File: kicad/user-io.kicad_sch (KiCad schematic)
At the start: 8 parts, among them J1 USB1, SW1 PTS815, U1 MIMXRT1171DVMAB, U2 MAYA-W166-00B

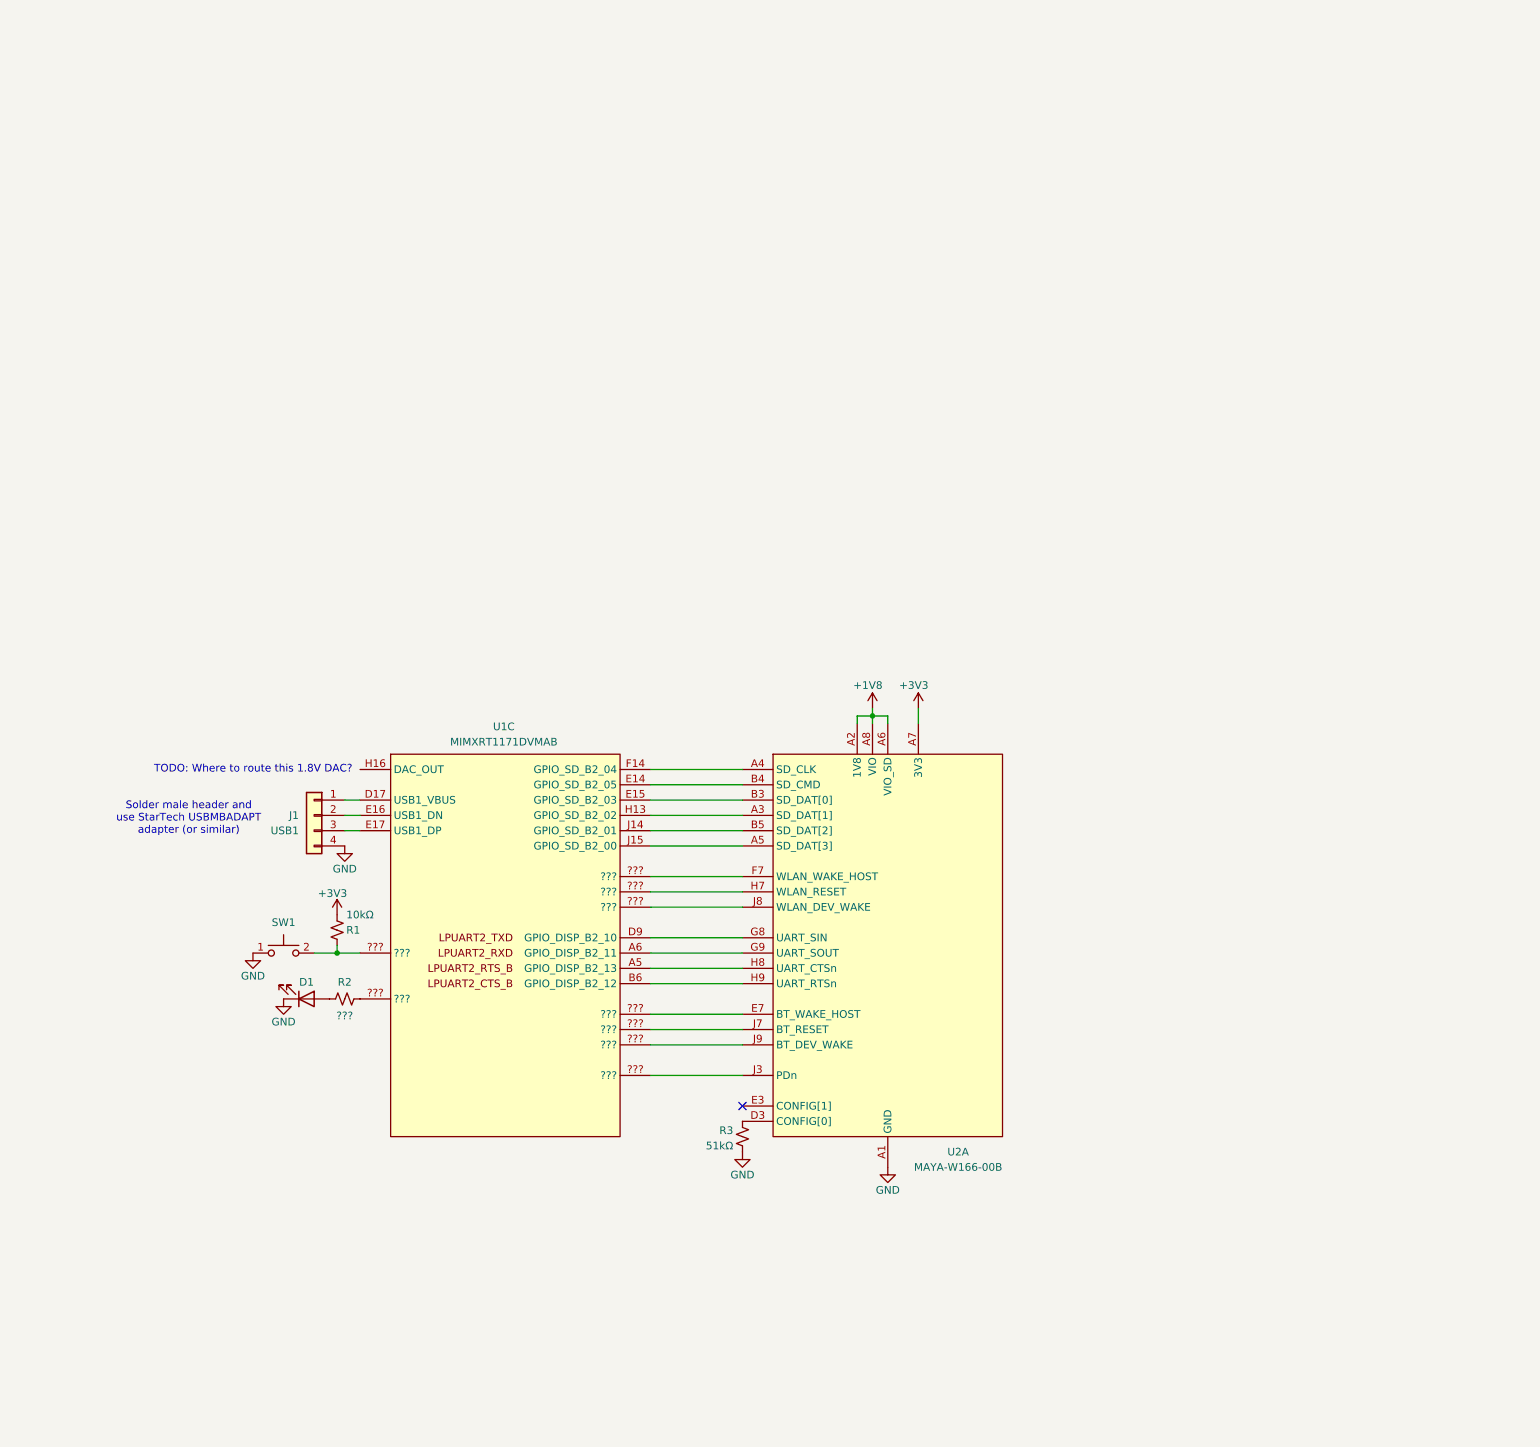
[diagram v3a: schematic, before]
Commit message: added IMU to schematic
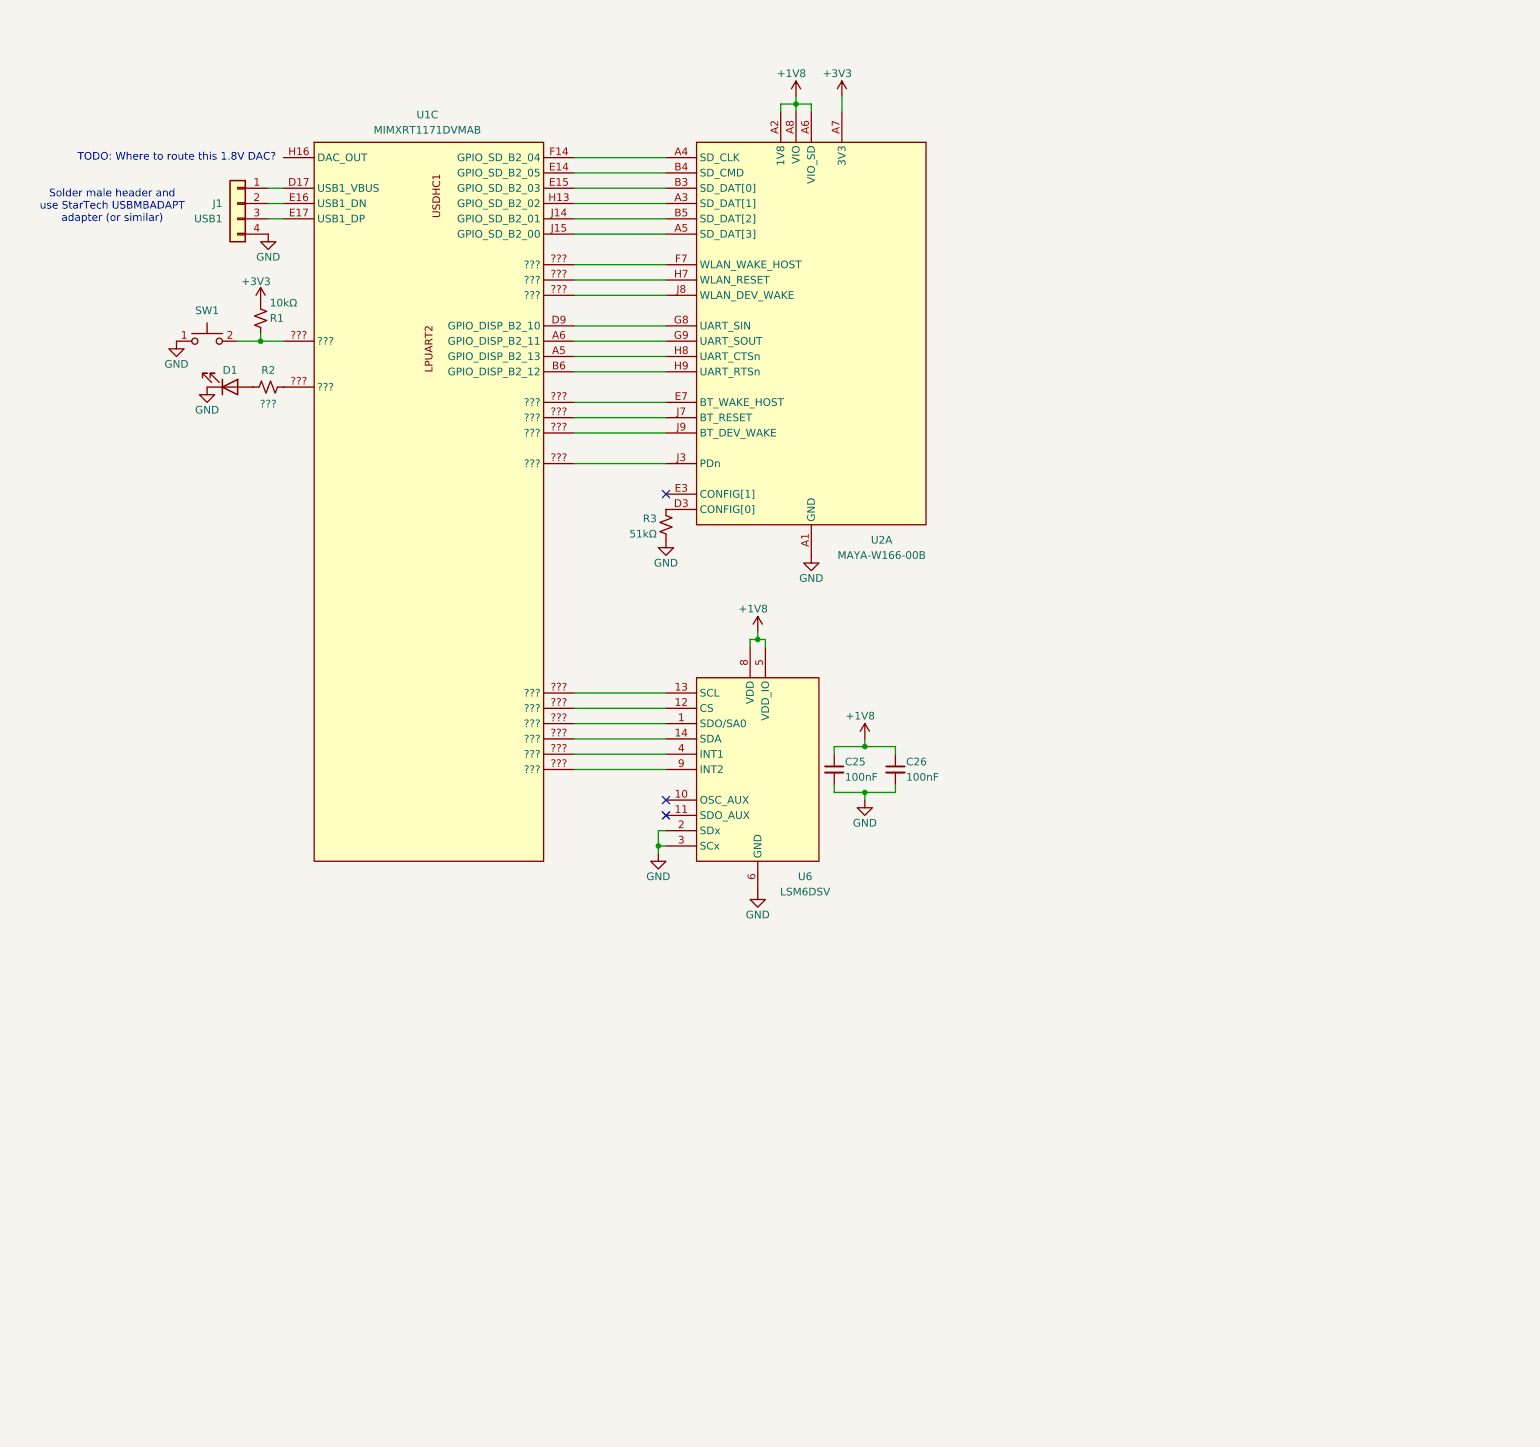
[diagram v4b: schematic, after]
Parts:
- added C25, C26: 100nF, symbol Device:C_Small
- added U6: LSM6DSV, symbol project_symbols:LSM6DSV
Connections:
- net +1V8: now also C25.1, C26.1, U6.5 (VDD_IO), U6.8 (VDD)
- net GND: now also C25.2, C26.2, U6.2 (SDx), U6.3 (SCx), U6.6 (GND), U6.7 (GND)
- new net: U1.???, U6.1 (SDO/SA0)
- new net: U1.???, U6.12 (CS)
- new net: U1.???, U6.13 (SCL)
- new net: U1.???, U6.14 (SDA)
- new net: U1.???, U6.4 (INT1)
- new net: U1.???, U6.9 (INT2)
- no-connect marks 1 -> 3
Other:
- moved on the sheet: D1, J1, R1, R2, R3, SW1, U2A

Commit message: added magnetometer to schematic
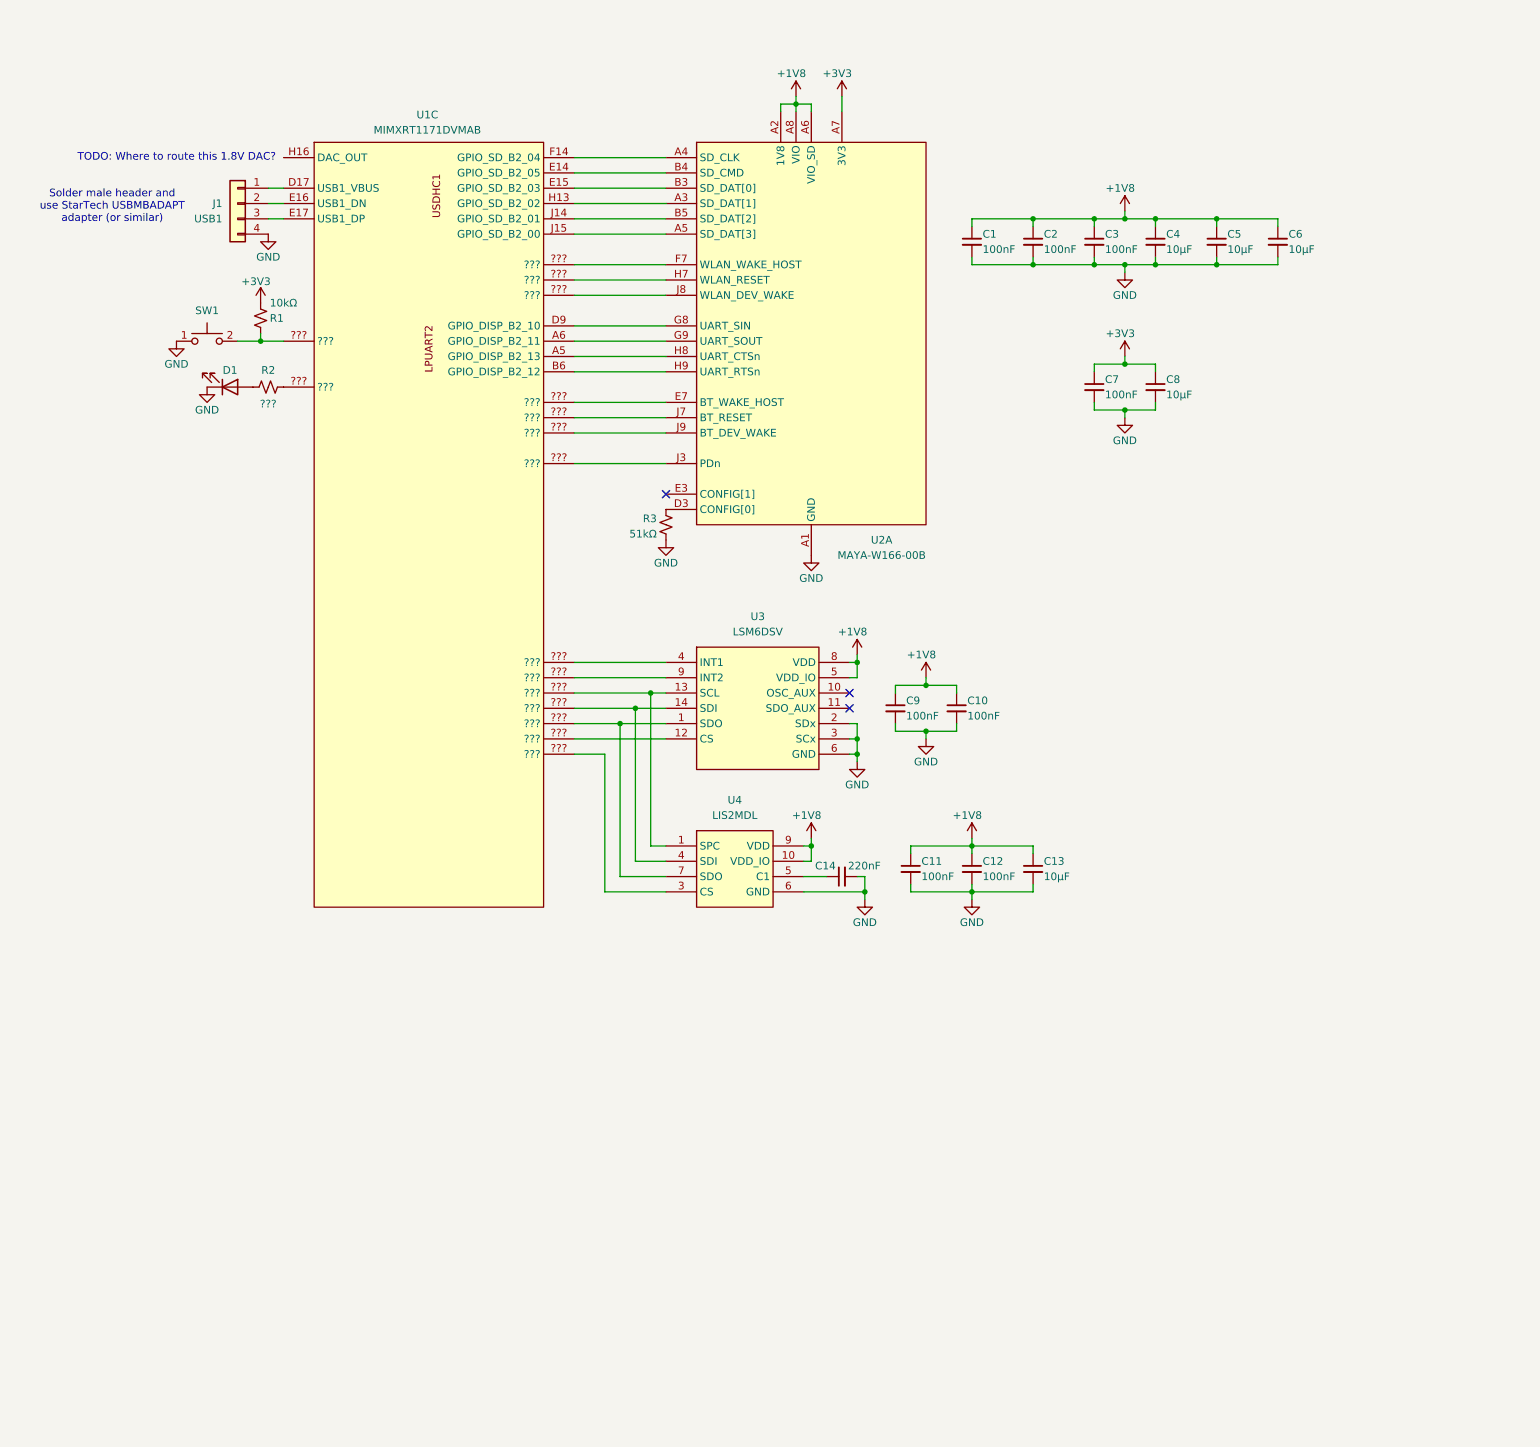
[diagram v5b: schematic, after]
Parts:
- removed U6: LSM6DSV, symbol project_symbols:LSM6DSV
- added C1, C11, C12, C2, C3, C7: 100nF, symbol Device:C_Small
- added C13, C4, C5, C6, C8: 10μF, symbol Device:C_Small
- added C14: 220nF, symbol Device:C_Small
- added U3: LSM6DSV, symbol project_symbols:LSM6DSV
- added U4: LIS2MDL, symbol project_symbols:LIS2MDL
- renumbered C26 to C10, C25 to C9
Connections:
- net +1V8: now also C1.1, C11.1, C12.1, C13.1, C2.1, C3.1, C4.1, C5.1, C6.1, U3.5 (VDD_IO), U3.8 (VDD), U4.10 (VDD_IO), U4.9 (VDD)
- net +3V3: now also C7.1, C8.1
- net GND: now also C1.2, C11.2, C12.2, C13.2, C14.2, C2.2, C3.2, C4.2, C5.2, C6.2, C7.2, C8.2, U3.2 (SDx), U3.3 (SCx), U3.6 (GND), U3.7 (GND), U4.6 (GND), U4.8 (GND)
- net at U1.???: now also U2.J9 (BT_DEV_WAKE)
- new net: U1.???, U3.1 (SDO), U4.7 (SDO)
- new net: U1.???, U3.12 (CS)
- new net: U1.???, U3.13 (SCL), U4.1 (SPC)
- new net: U1.???, U3.14 (SDI), U4.4 (SDI)
- new net: U1.???, U3.4 (INT1)
- new net: U1.???, U3.9 (INT2)
- new net: C14.1, U4.5 (C1)
- new net: U1.???, U4.3 (CS)
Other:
- moved on the sheet: C10, C9

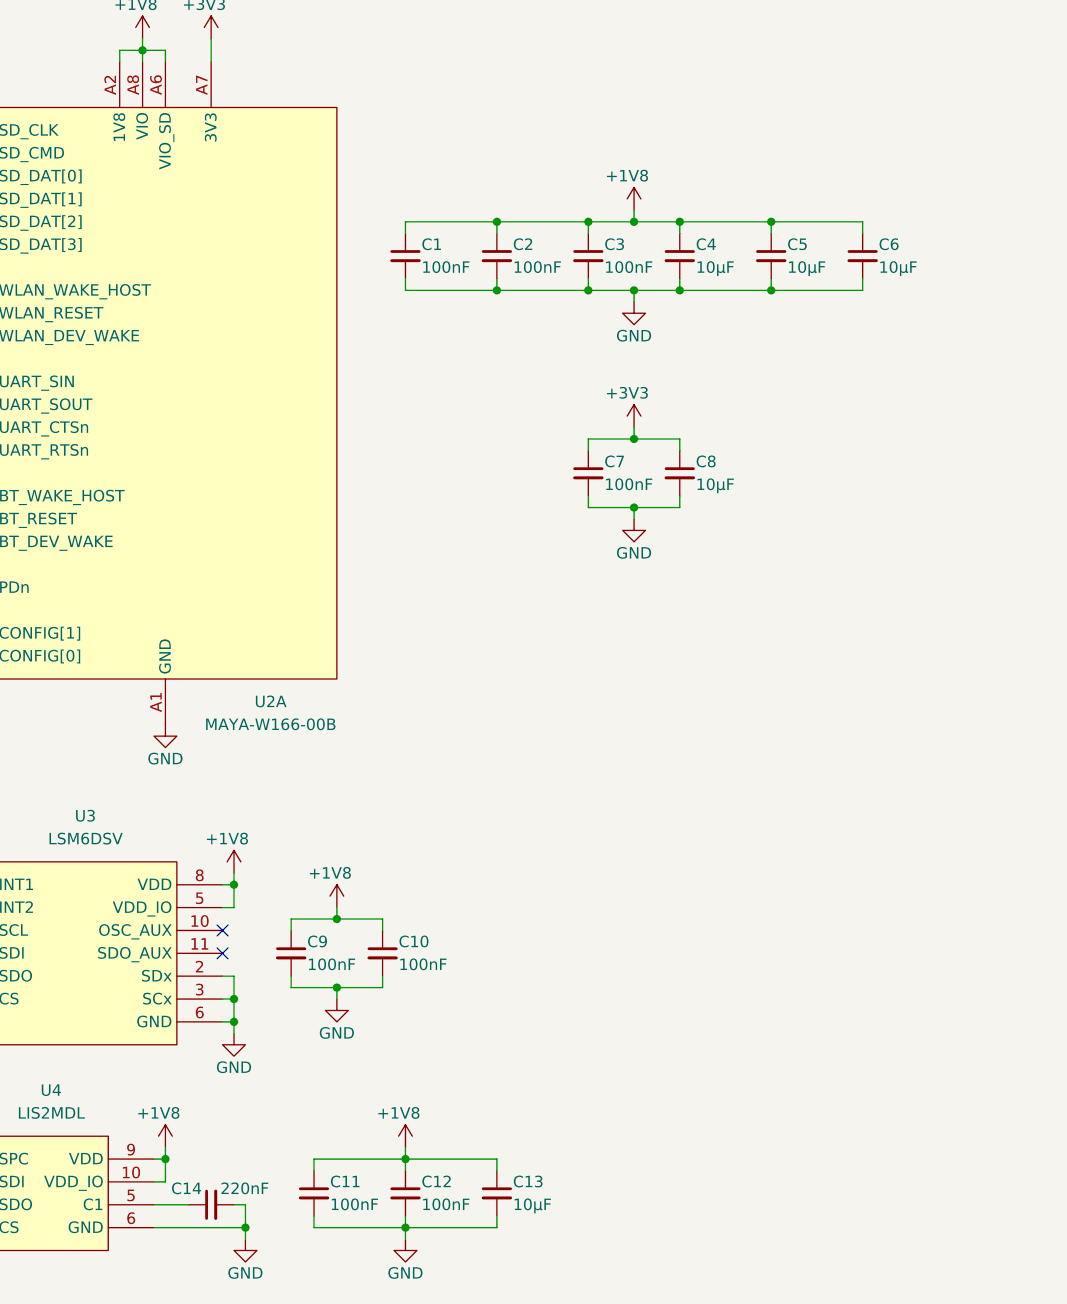
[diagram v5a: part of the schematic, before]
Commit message: added bypass caps
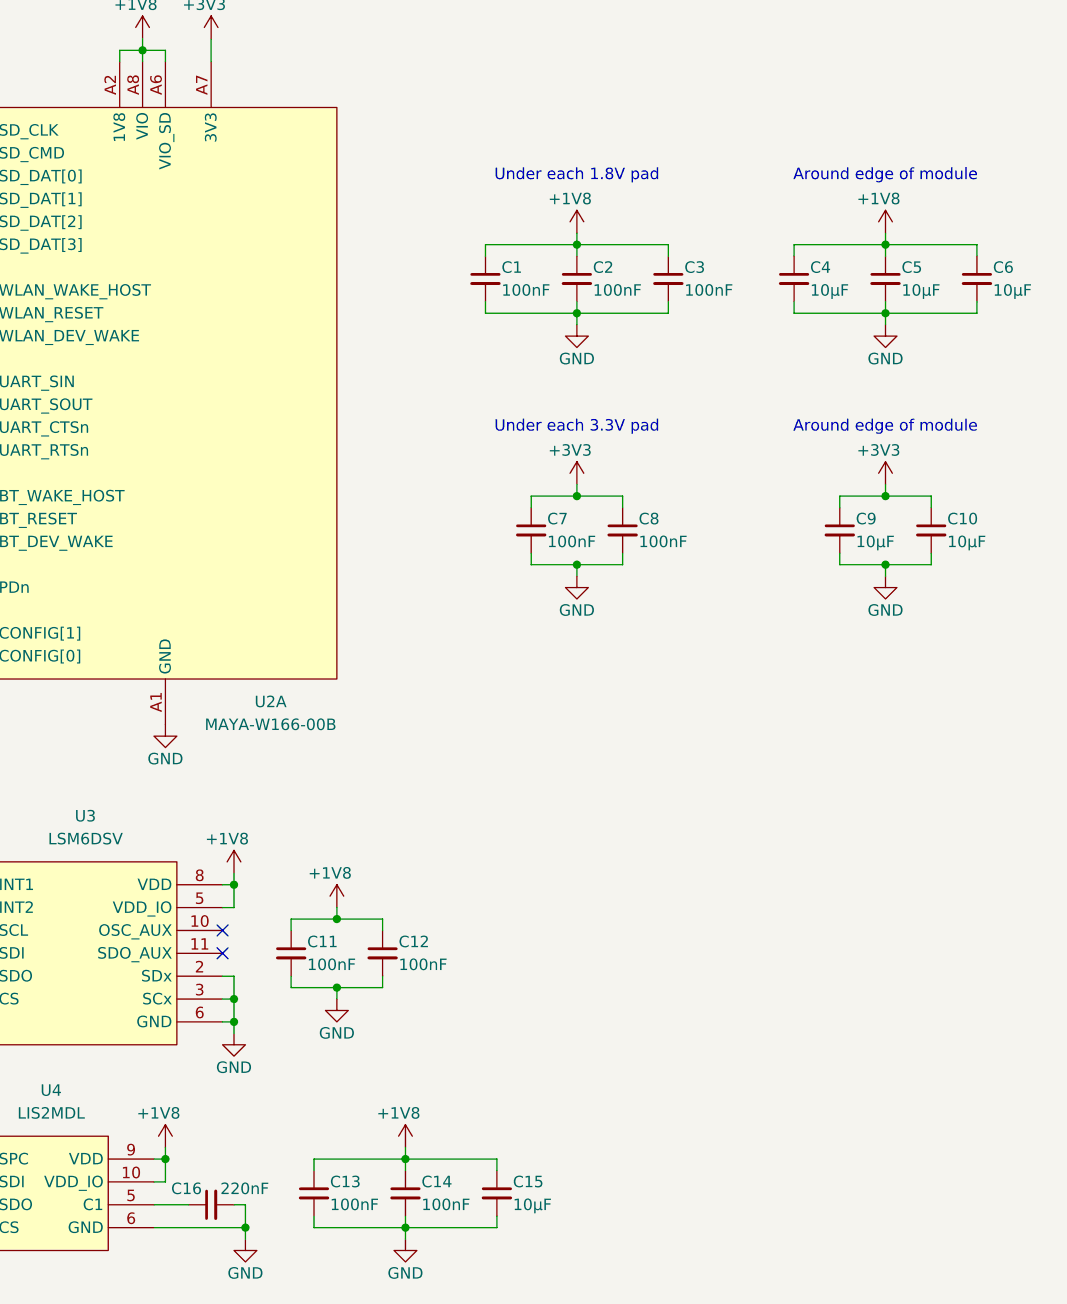
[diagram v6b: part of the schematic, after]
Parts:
- added C10, C9: 10μF, symbol Device:C_Small
- C8: value 10μF -> 100nF
- renumbered C9 to C11, C10 to C12, C11 to C13, C12 to C14, C13 to C15, C14 to C16
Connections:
- net +3V3: now also C10.1, C9.1
- net GND: now also C10.2, C9.2
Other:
- note added: "Around edge of module"
- note added: "Under each 1.8V pad"
- note added: "Under each 3.3V pad"

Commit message: added KL26 (DAPLink HIC) to schematic
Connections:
- net +3V3: no longer R1.2
- new net ???: R1.2
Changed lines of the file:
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@@
 			)
 		)
-		(property "Value" "+3V3"
+		(property "Value" "???"
 			(at 91.948 61.214 0)
 			(show_name no)
